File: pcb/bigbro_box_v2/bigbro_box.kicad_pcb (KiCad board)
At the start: 2 copper layers, 112 x 55 mm, 43 parts, among them J1 CT_AMP, J2 Display, J3 Mains, J4 UART flashing, J5 Conn_01x02, J6 Relay, K1 G5LE-1, Q1 ADC114YUQ, Q2 Q_NMOS_GDS, Q3 MMBT3906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

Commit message: Change to RDM6300, etc.
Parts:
- removed U6: 74LVC1T45, Package_TO_SOT_SMD:SOT-23-6
- added D2: LED, LED_SMD:LED_0603_1608Metric, F.Cu at (106.4, 112.3)
- added D3: LED, LED_SMD:LED_0603_1608Metric, F.Cu at (135.4, 88.1)
- added Q2: MMBT3904, Package_TO_SOT_SMD:SOT-23, F.Cu at (142.8, 88.4)
- added R9: 330, Resistor_SMD:R_0603_1608Metric, F.Cu at (135.4, 90.7)
- added TP11: TestPoint, TestPoint:TestPoint_Keystone_5000-5004_Miniature, F.Cu at (109.5, 62.7)
- D1: value D_Small -> 1N4148
- Q1: value ADC114YUQ -> MMBT3904; footprint Package_TO_SOT_SMD:SOT-363_SC-70-6 -> Package_TO_SOT_SMD:SOT-23
- Q3: renamed from Q2; value Q_NMOS_GDS -> BSS138
- R6: value 10k -> 1K; footprint Resistor_SMD:R_0603_1608Metric_Pad0.98x0.95mm_HandSolder -> Resistor_SMD:R_0603_1608Metric
- U5: value RF125-PS -> RDM6300; footprint mylib:rf125ps -> modules:RDM6300_B38.5x18.2mm
- moved U5 80.5 mm to (131.1, 111.3), turned to 0 degrees
- moved C3 70.2 mm to (155.3, 99.6)
- moved J5 63.4 mm to (123.0, 111.5)
- moved J6 12.3 mm to (71.9, 107.2), turned to 90 degrees
- moved J3 8.67 mm to (71.8, 81.0), turned to 90 degrees
- moved R6 7.62 mm to (110.8, 109.5), turned to 0 degrees
- renumbered Q3 to Q4
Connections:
- D1 pad 2: Net-(D1-Pad2) -> Net-(D1-A)
- F1 pad 1: /L_in -> Net-(J3-Pin_2)
- J3 pad 1: /L_in -> Net-(J3-Pin_1)
- J3 pad 2: /N_in -> Net-(J3-Pin_2)
- J5 pad 1: Net-(J5-Pad1) -> Net-(J5-Pin_1)
- J5 pad 2: Net-(J5-Pad2) -> Net-(J5-Pin_2)
- J6 pad 1: /NO -> /NC
- J6 pad 3: /NC -> /NO
- K1 pad 2: Net-(D1-Pad2) -> Net-(D1-A)
- PS1 pad 2: /N_in -> Net-(J3-Pin_1)
- Q3 pad 2: Net-(D1-Pad2) -> Net-(D1-A)
- R6 pad 1: /relay_gpio -> Net-(D2-K)
- R6 pad 2: GND -> Net-(D1-A)
- U4 pad 10: (no net) -> unconnected-(U4-Pad10)
- U4 pad 11: (no net) -> unconnected-(U4-Pad11)
- U4 pad 12: (no net) -> +3V3
- U4 pad 13: (no net) -> +3V3
- U4 pad 8: (no net) -> GND
- U4 pad 9: (no net) -> GND
- U5 pad 1: GND -> Net-(J5-Pin_1)
- U5 pad 2: +5V -> Net-(J5-Pin_2)
- U5 pad 3: Net-(U5-Pad3) -> GND
- U5 pad 4: unconnected-(U5-Pad4) -> +5V
- U5 pad 6: Net-(J5-Pad2) -> ESP_RFID_TX
- U5 pad 7: Net-(J5-Pad1) -> unconnected-(U5-RX-Pad7)
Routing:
- net /L_in: track 16.3 -> 0.00 mm
- net /N_in: track 15.7 -> 0.00 mm
- net /NC: track 38.8 -> 25.0 mm
- net /COM: track 66.4 -> 52.7 mm
- net /NO: track 38.8 -> 25.1 mm
- net Net-(D1-Pad2): track 5.67 -> 0.00 mm
- net Net-(J3-Pin_2): track 0.00 -> 5.20 mm

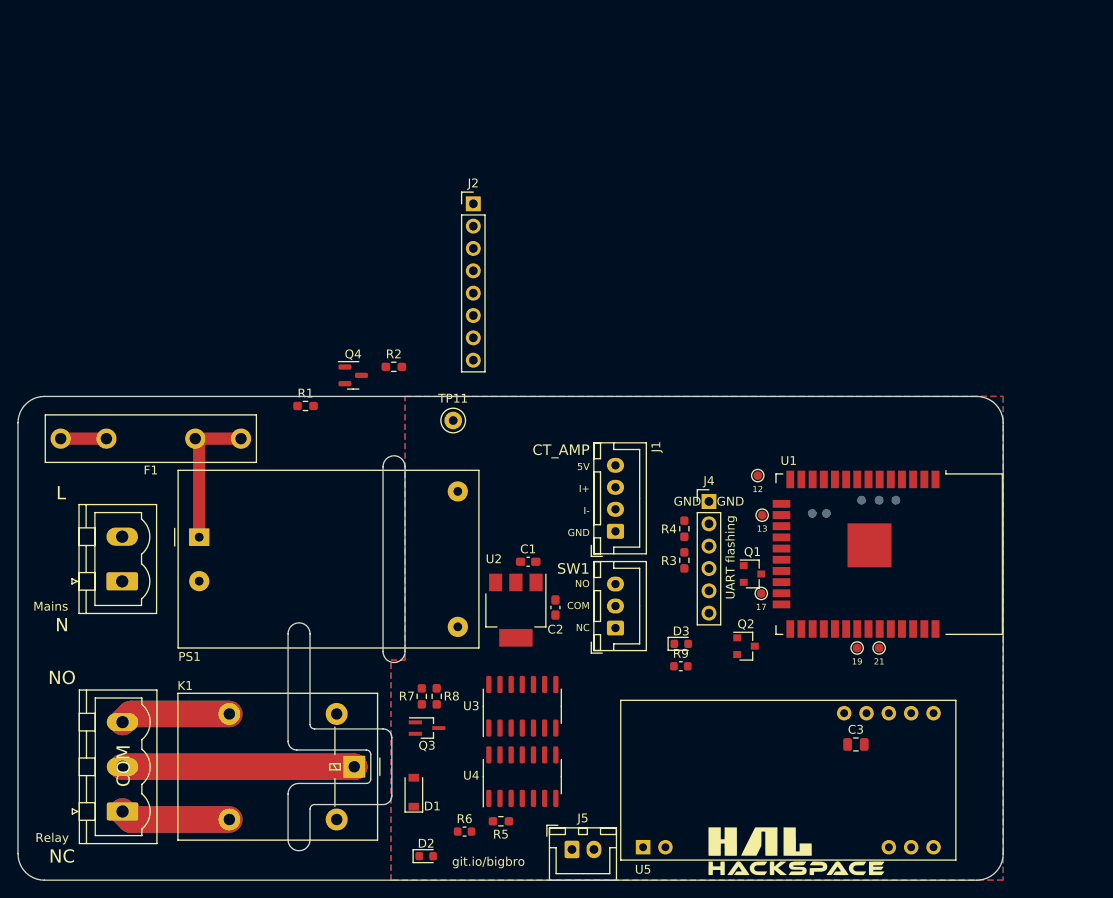
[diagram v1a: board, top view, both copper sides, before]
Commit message: New fuse holder, rearrange footprints.
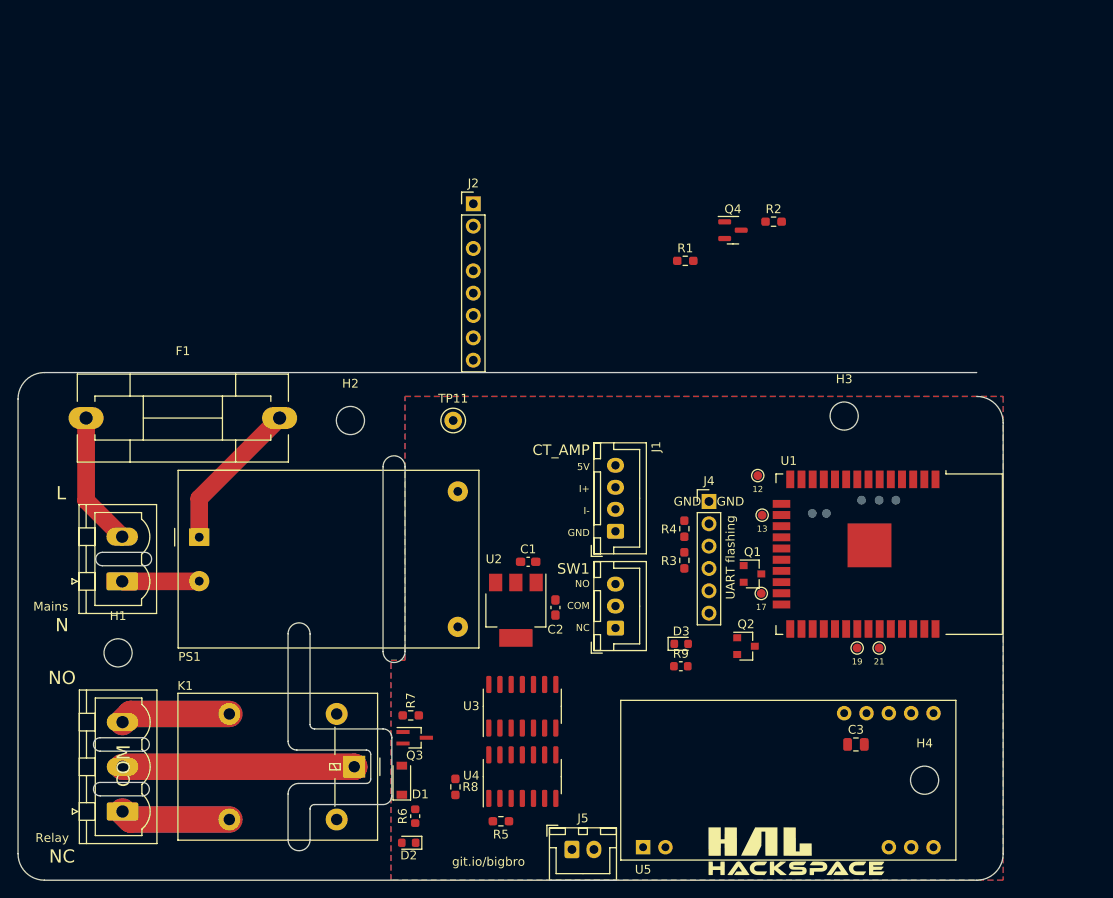
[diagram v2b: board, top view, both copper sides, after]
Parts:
- added H1: MountingHole, MountingHole:MountingHole_3.2mm_M3, F.Cu at (71.4, 89.2)
- added H2: MountingHole, MountingHole:MountingHole_3.2mm_M3, F.Cu at (97.8, 62.7)
- added H3: MountingHole, MountingHole:MountingHole_3.2mm_M3, F.Cu at (153.9, 62.2)
- added H4: MountingHole, MountingHole:MountingHole_3.2mm_M3, F.Cu at (163.1, 103.6)
- F1: footprint Fuse:Fuseholder_Littelfuse_445_030_series_5x20mm -> modules:Fuseholder5x20_horiz_SemiClosed_Casing10x25mm
- moved Q4 46.2 mm to (141.3, 41.1)
- moved R1 46.2 mm to (135.9, 44.6)
- moved R2 46.2 mm to (145.9, 40.1)
- moved R8 10.5 mm to (109.7, 104.4)
- moved R6 5.88 mm to (105.2, 107.7), turned to 90 degrees
- moved F1 3.72 mm to (67.7, 62.5)
- moved R7 2.50 mm to (104.6, 96.3), turned to 180 degrees
- moved D2 2.50 mm to (104.4, 110.7), turned to 180 degrees
- moved D1 1.93 mm to (103.6, 103.6)
- moved Q3 1.79 mm to (105.1, 98.8)
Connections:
- U3 pad 1: /~{relay_gpio} -> /Relay_trig
- U3 pad 10: /relay -> /Relay_reset
- U3 pad 11: Net-(U3-Pad11) -> /Relay_trig
- U3 pad 12: /relay -> /card_switch
- U3 pad 13: /Relay_reset -> /relay_gpio
- U3 pad 2: /~{card_switch} -> Net-(U3-Pad2)
- U3 pad 3: /Relay_reset -> /relay
- U3 pad 4: /Relay_trig -> Net-(U3-Pad2)
- U3 pad 5: /card_switch -> /relay
- U3 pad 6: /relay_gpio -> /Relay_reset
- U3 pad 8: /Relay_trig -> /~{relay_gpio}
- U3 pad 9: Net-(U3-Pad11) -> /~{card_switch}
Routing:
- net Net-(J3-Pin_2): track 5.20 -> 15.2 mm
- net Net-(J3-Pin_1): track 0.08 -> 8.85 mm
- net Net-(PS1-AC/L): track 16.6 -> 17.3 mm
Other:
- board size 112 x 55 mm -> 112 x 57.7 mm

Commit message: Optimize allocation of gates.
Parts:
- SW1: value SW_SPDT -> SW_SPST; footprint Connector_JST:JST_XH_B3B-XH-A_1x03_P2.50mm_Vertical -> Connector_JST:JST_XH_B2B-XH-A_1x02_P2.50mm_Vertical
- moved TP11 50.8 mm to (160.3, 62.2)
- moved C2 24.9 mm to (116.8, 59.4)
- moved U2 22.5 mm to (111.3, 62.5), turned to 0 degrees
- moved C1 21.0 mm to (104.6, 62.6), turned to 90 degrees
- moved R5 18.5 mm to (133.2, 105.4)
- moved J2 18.4 mm to (121.7, 22.6)
- moved SW1 12.3 mm to (122.9, 97.5), turned to 0 degrees
- moved J1 12.0 mm to (116.6, 79.1)
- moved R8 10.9 mm to (106.4, 94.0), turned to 0 degrees
- moved Q2 10.8 mm to (132.1, 90.3)
- moved R9 10.8 mm to (124.7, 92.6)
- moved TP10 10.8 mm to (147.3, 73.7)
- moved TP3 10.8 mm to (139.7, 75.2)
- moved TP5 10.8 mm to (144.8, 90.5)
- moved TP6 10.8 mm to (147.3, 90.5)
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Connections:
- SW1 pad 1: unconnected-(SW1-A-Pad1) -> /card_switch
- U3 pad 1: /Relay_trig -> /card_switch
- U3 pad 10: /Relay_reset -> /relay
- U3 pad 11: /Relay_trig -> unconnected-(U3-Pad11)
- U3 pad 12: /card_switch -> +3V3
- U3 pad 13: /relay_gpio -> +3V3
- U3 pad 2: Net-(U3-Pad2) -> /card_switch
- U3 pad 3: /relay -> /~{relay_gpio}
- U3 pad 4: Net-(U3-Pad2) -> Net-(U3-Pad4)
- U3 pad 8: /~{relay_gpio} -> /Relay_trig
- U3 pad 9: /~{card_switch} -> Net-(U3-Pad4)
- U4 pad 1: /card_switch -> /relay_gpio
- U4 pad 10: unconnected-(U4-Pad10) -> /Relay_trig
- U4 pad 11: unconnected-(U4-Pad11) -> /Relay_reset
- U4 pad 12: +3V3 -> /~{relay_gpio}
- U4 pad 13: +3V3 -> /~{card_switch}
- U4 pad 2: /card_switch -> /relay_gpio
- U4 pad 3: /~{relay_gpio} -> /~{card_switch}
- U4 pad 4: /~{card_switch} -> unconnected-(U4-Pad4)
- U4 pad 5: /relay_gpio -> GND
- U4 pad 6: /relay_gpio -> GND
- U4 pad 8: GND -> /card_switch
- U4 pad 9: GND -> /relay_gpio
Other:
- board size 112 x 57.7 mm -> 102 x 58 mm

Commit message: Change current sense to single pin.
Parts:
- J1: value CT_AMP -> Current Sense; footprint Connector_JST:JST_XH_B4B-XH-A_1x04_P2.50mm_Vertical -> Connector_JST:JST_XH_B3B-XH-A_1x03_P2.50mm_Vertical
- J5: value Conn_01x02 -> RFID
- Q3: footprint Package_TO_SOT_SMD:SOT-323_SC-70_Handsoldering -> Package_TO_SOT_SMD:SOT-323_SC-70
- R1, R2, R3, R4, R5, R7, R8: footprint Resistor_SMD:R_0603_1608Metric_Pad0.98x0.95mm_HandSolder -> Resistor_SMD:R_0603_1608Metric
- SW1: value SW_SPST -> Card switch
- moved J2 65.3 mm to (115.8, 87.6), turned to 180 degrees
- moved R2 36.0 mm to (118.1, 63.0)
- moved J1 35.4 mm to (147.4, 61.7), turned to 0 degrees
- moved Q4 33.9 mm to (118.1, 65.9), turned to -90 degrees
- moved TP11 27.3 mm to (180.3, 43.7)
- moved Q2 26.8 mm to (138.2, 64.3)
- moved R1 24.8 mm to (121.4, 64.8)
- moved Q1 20.3 mm to (142.5, 64.2)
- moved R3 19.4 mm to (134.4, 63.5)
- moved J4 13.5 mm to (128.8, 60.5), turned to 90 degrees
- moved R4 13.1 mm to (129.3, 64.5)
- moved H3 8.95 mm to (162.8, 61.2)
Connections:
- net /I_Sens- renamed /CurrentSense
- J1 pad 1: GND -> +5V
- J1 pad 3: /I_Sens+ -> GND
- J2 pad 1: Display_Led -> +3V3
- J2 pad 2: Display_SCk -> GND
- J2 pad 3: Display_SDA -> Display_CS
- J2 pad 4: Display_A0 -> Display_Reset
- J2 pad 5: Display_Reset -> Display_A0
- J2 pad 6: Display_CS -> Display_SDA
- J2 pad 7: GND -> Display_SCk
- J2 pad 8: +3V3 -> Display_Led
- U1 pad 4: /I_Sens+ -> unconnected-(U1-SENSOR_VP-Pad4)
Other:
- board text removed: "5V"
- board text removed: "GND"
- board text removed: "GND GND"
- board text removed: "I+"
- board text removed: "I-"

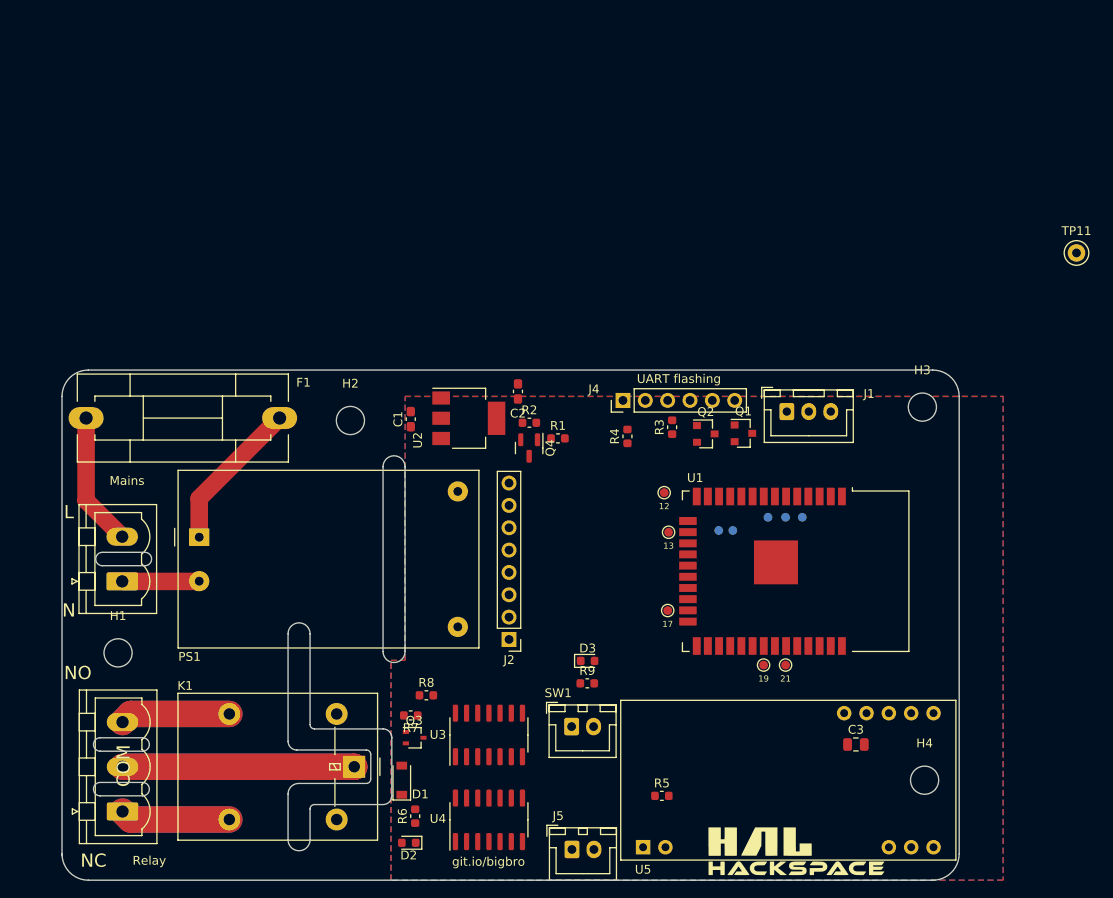
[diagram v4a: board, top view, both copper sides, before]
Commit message: Add 3D model for RDM6300 socket.
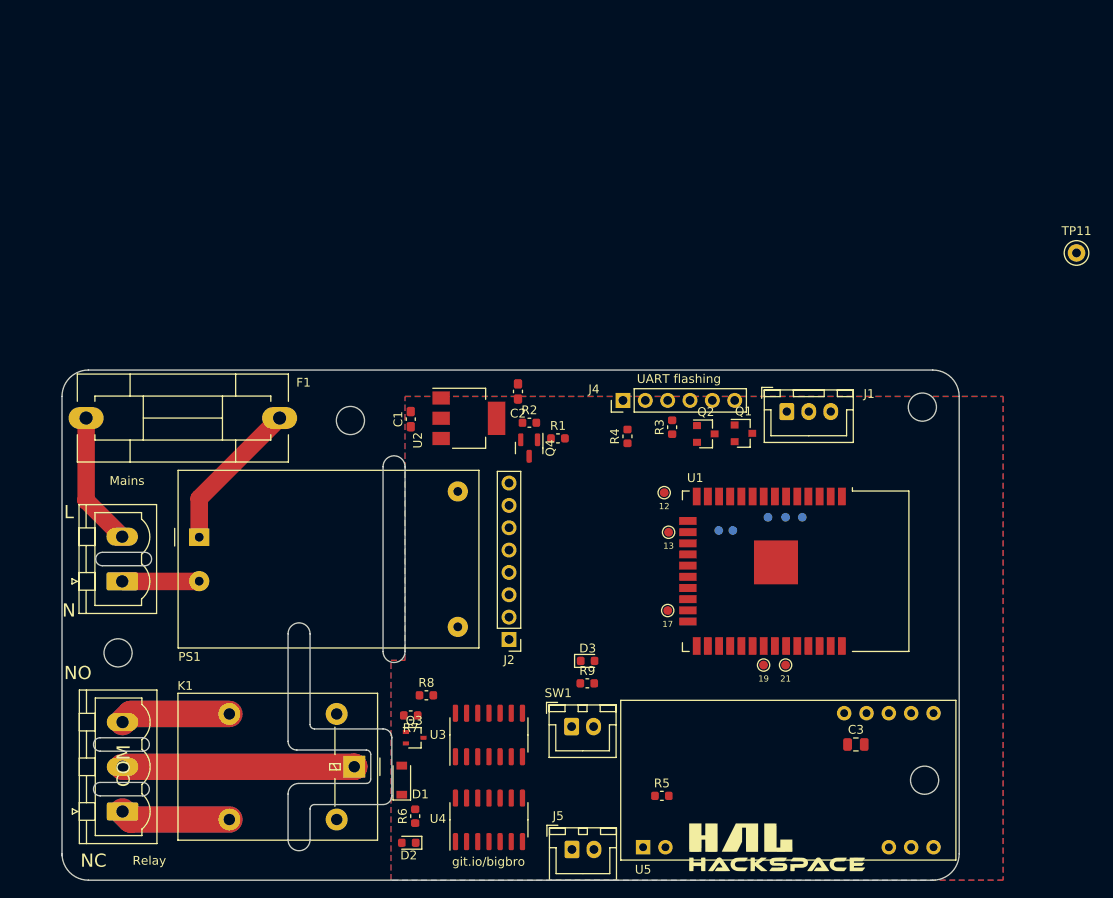
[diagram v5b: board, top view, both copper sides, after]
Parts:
- moved G*** 2.24 mm to (146.3, 111.3)
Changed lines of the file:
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@@
     (property "ki_keywords" "mounting hole")
     (attr exclude_from_pos_files)
-    (fp_text reference "H1" (at 0 -4.2) (layer "F.SilkS")
+    (fp_text reference "H1" (at 4.318 -2.286) (layer "F.SilkS") hide
         (effects (font (size 1 1) (thickness 0.15)))
     )
@@
   )
   (footprint "hal9k-graphics:hal9k-logo_20mm" (layer "F.Cu")
-    (at 148.5 111.7)
+    (at 146.304 111.252)
     (attr board_only exclude_from_pos_files exclude_from_bom)
     (fp_text reference "G***" (at 0 0) (layer "F.SilkS") hide
@@
     (pad "10" thru_hole circle (at 22.86 -15.24) (size 1.65 1.65) (drill 0.9) (layers "*.Cu" "*.Mask")
       (net 1 "+5V") (pinfunction "5V") (pintype "power_in"))
+    (model "${KIPRJMOD}/lib/3D/RDM6300-socket.step"
+      (offset (xyz 0 0 0))
+      (scale (xyz 1 1 1))
+      (rotate (xyz 0 0 0))
+    )
   )
   (footprint "Package_TO_SOT_SMD:SOT-23" (layer "F.Cu")
@@
     (property "ki_keywords" "mounting hole")
     (attr exclude_from_pos_files)
-    (fp_text reference "H2" (at 0 -4.2) (layer "F.SilkS")
+    (fp_text reference "H2" (at 0 -4.2) (layer "F.SilkS") hide
         (effects (font (size 1 1) (thickness 0.15)))
     )
@@
     (property "ki_keywords" "mounting hole")
     (attr exclude_from_pos_files)
-    (fp_text reference "H3" (at 0 -4.2) (layer "F.SilkS")
+    (fp_text reference "H3" (at -4.318 -3.048) (layer "F.SilkS") hide
         (effects (font (size 1 1) (thickness 0.15)))
     )
@@
     (property "ki_keywords" "mounting hole")
     (attr exclude_from_pos_files)
-    (fp_text reference "H4" (at 0 -4.2) (layer "F.SilkS")
+    (fp_text reference "H4" (at 0 -4.2) (layer "F.SilkS") hide
         (effects (font (size 1 1) (thickness 0.15)))
     )
